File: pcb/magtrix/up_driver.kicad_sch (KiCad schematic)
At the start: 4 parts, among them Q17 BUK6D120-60PX

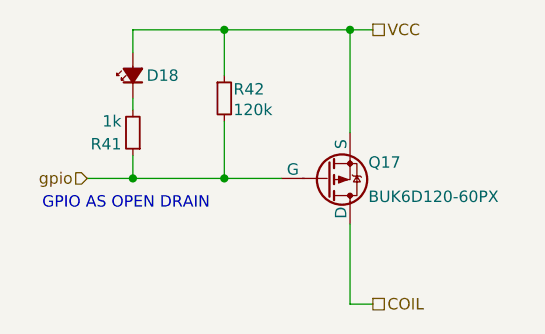
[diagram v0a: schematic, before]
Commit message: Finished schematics and footprints, need to redo the placement
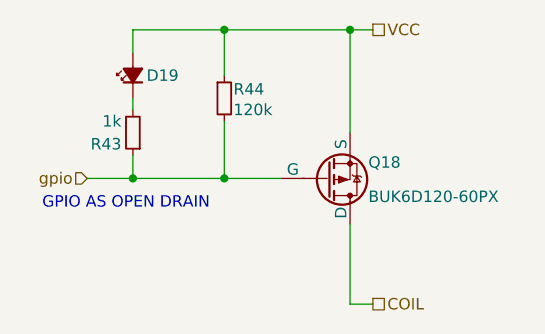
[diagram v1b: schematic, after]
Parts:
- Q18: renamed from Q17; footprint (none) -> TRANSISTOR_PMOS:BUK6D12060PX; MFR (none) -> BUK6D120-60PX; MOUSER (none) -> 771-BUK6D120-60PX
- renumbered D18 to D19, R41 to R43, R42 to R44
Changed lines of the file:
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@@
 		(on_board yes)
 		(dnp no)
-		(property "Reference" "R42"
+		(property "Reference" "R44"
 			(at 61.976 40.894 0)
 			(effects
@@
 		(on_board yes)
 		(dnp no)
-		(property "Reference" "Q17"
+		(property "Reference" "Q18"
 			(at 76.962 49.022 0)
 			(effects
@@
 			)
 		)
-		(property "Footprint" ""
+		(property "Footprint" "TRANSISTOR_PMOS:BUK6D12060PX"
 			(at 78.74 47.244 0)
 			(effects
@@
 		(property "Sim.Pins" "1=D 2=G 3=S"
 			(at 73.66 64.77 0)
+			(effects
+				(font
+					(size 1.27 1.27)
+				)
+				(hide yes)
+			)
+		)
+		(property "MFR" "BUK6D120-60PX "
+			(at 73.66 49.53 0)
+			(effects
+				(font
+					(size 1.27 1.27)
+				)
+				(hide yes)
+			)
+		)
+		(property "MOUSER" "771-BUK6D120-60PX "
+			(at 73.66 49.53 0)
 			(effects
 				(font
@@
 			(project "magtrix"
 				(path "/11af7b42-8094-4ca6-9444-8e07a1921bec/0b4f6fb6-2c65-403c-8b01-28a6f9e19105"
-					(reference "Q17")
+					(reference "Q18")
 					(unit 1)
 				)
@@
 				(path "/11af7b42-8094-4ca6-9444-8e07a1921bec/c3e2f809-0283-4cab-b969-e6565462d611"
 					(reference "Q32")
+					(unit 1)
+				)
+				(path "/11af7b42-8094-4ca6-9444-8e07a1921bec/c5bf1ec6-a44d-43ed-bb37-93f7abbce5ff"
+					(reference "Q17")
 					(unit 1)
 				)
@@
 		(on_board yes)
 		(dnp no)
-		(property "Reference" "D18"
+		(property "Reference" "D19"
 			(at 52.324 39.37 90)
 			(effects
@@
 		(on_board yes)
 		(dnp no)
-		(property "Reference" "R41"
+		(property "Reference" "R43"
 			(at 49.53 46.99 0)
 			(effects
